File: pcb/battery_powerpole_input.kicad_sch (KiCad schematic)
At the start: 7 parts, among them J1 1377G12-BK, J2 MCV 1,5/ 2-GF-3,81

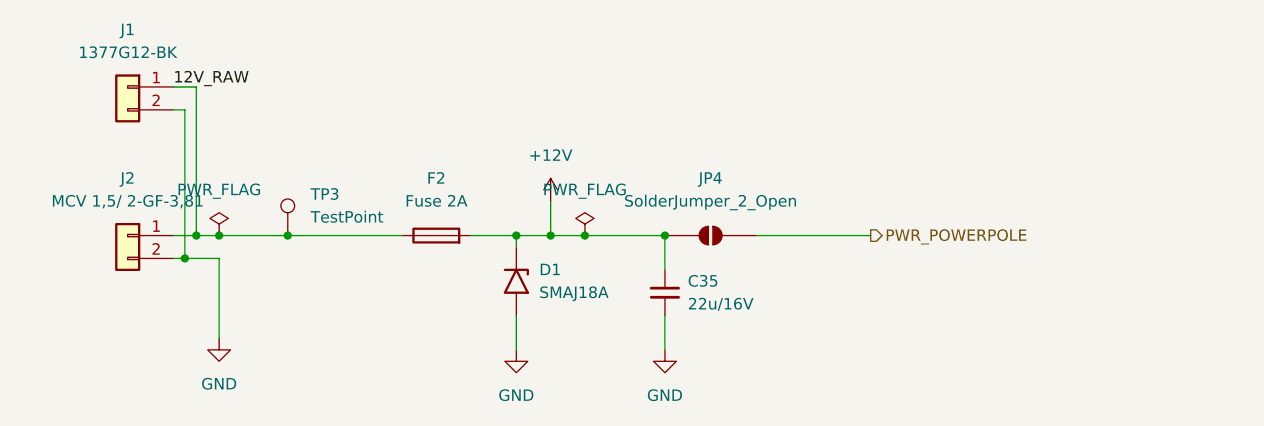
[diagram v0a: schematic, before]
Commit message: Add TPS2121 Stage 2/3: USB-vs-battery priority muxing on 5V and 3.3V rails
power.kicad_sch:
- U14 (TPS2121RUXR): 5V rail mux. IN1=BATT_5V_REG (priority), IN2=USB_5V_IN,
  OUT=+5V. PR1 tied to IN1, CP2/OV1/OV2 to GND (VREF priority mode -- battery
  always wins when present, no voltage-comparison ambiguity between two
  nominally-5V sources). ILM set via R26 (30.1k, ~3.5A class, sized with
  margin above the 2A SA818 budget for TX current transients). SS via C42
  (0.01uF). ST feeds the battery/USB detect logic below.
- U13 (TPS2121RUXR): 3.3V rail mux, same configuration. IN1=BATT_3.3V_REG,
  IN2=USB_3.3V_IN, OUT=+3.3V. ILM via R25 (80.6k, ~1.5A class, vs 1A
  peripheral budget). SS via C41.
- U1 (74LVC1G08): AND-gates U13.ST and U14.ST (each pulled up individually
  via R27/R28, 10k to +3.3V, since ST is open-drain) into PWR_ON_BATTERY --
  high only when both rails are confirmed running from battery, low if
  either has fallen back to USB. Output exposed as a new Power sheet pin.

foxhunt1.kicad_sch: bridges PWR_ON_BATTERY (Power sheet) to the new
IO_IN_ON_BATT input on the mcu-esp32 sheet, and USB_3.3V_IN/USB_5V_IN
(Power sheet) to USB_3.3V/USB_5V (USB-C sheet) -- these were previously
unconnected placeholder labels.

mcu-esp32.kicad_sch: IO_IN_ON_BATT wired to U8 pin 35 (GPIO42), the one
GPIO the pinout doc had marked as still spare.

kicad_gx_library: TPS2121RUXR symbol fix (one OUT pin marked passive
instead of output, since the two physical OUT pins are meant to be tied
together -- avoids an ERC driver-conflict false positive).

power_regulation.kicad_sch, battery_18650_input.kicad_sch,
battery_powerpole_input.kicad_sch, foxhunt1.kicad_pro: incidental KiCad
save cleanup, no circuit changes (verified via orphan/short checks and
netlist diff -- same components as before).

Fully traced pin-by-pin: both mux dividers/ILM/SS wiring, the battery-vs-
USB source assignment on each rail (not swapped), the AND-gate inputs,
and all three cross-sheet bridges. 0 new orpha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
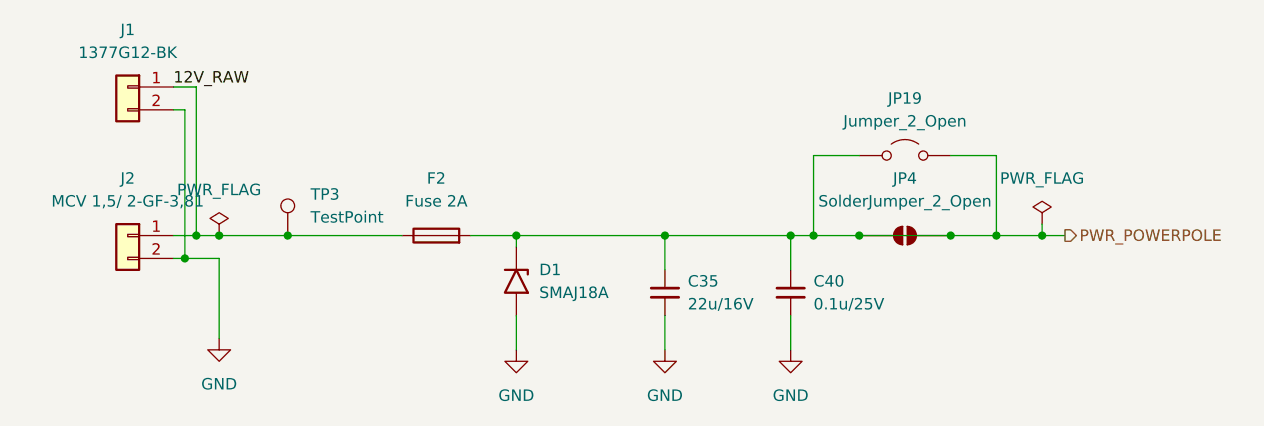
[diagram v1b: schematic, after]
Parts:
- added C40: 0.1u/25V, Capacitor_SMD:C_0603_1608Metric, symbol Device:C_Small
- added JP19: Jumper_2_Open, symbol Jumper:Jumper_2_Open
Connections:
- net +12V is gone; now on net PWR_POWERPOLE: C35.1, D1.1 (A1), F2.2, JP4.1 (A)
- net GND: now also C40.2
- net PWR_POWERPOLE: now also C40.1, JP19.1 (A), JP19.2 (B)
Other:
- moved on the sheet: JP4

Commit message: Full re-annotation, BOM audit fixes, Stage-1 ILM resize, and PCB reset
Schematic: re-annotated reference designators project-wide (3rd pass) --
every real component's designator has shifted since the last commit.
Fixed BOM gaps found by the fresh audit: U13 (CH340C) sourcing fields,
R7's Manf typo (YAGE -> YAGEO), R5/R8/R14 missing LCSC Part#s, and
normalized U1/U2/U3 (TPS2121RUXR) field names from easyeda2kicad's
defaults (Manufacturer/LCSC Part) to this project's convention
(Manf/LCSC Part #). Resized Stage 1's ILM resistor (R8) from 51.1k to
30.1k -- the prior value undersized the current limit for carrying both
downstream rails' combined battery-side current.

pcb/foxhunt1.kicad_pcb: cleared all footprints. No board layout has
started yet; this reflects that accurately rather than carrying stale
placements from before the schematic settled.

_agent_tasks/bom_property_audit.md: new reusable playbook for this BOM
audit (method, standing exceptions, reporting format), so future passes
don't have to re-derive the approach each time.

_docs/sourcing/task1_lcsc_crossreference.md: replaced stale results
(referencing pre-renumbering designators) with the current audit's
findings. One open item remains: the current-sense shunt's footprint
implies Vishay pad geometry but the sourced part is Milliohm-brand,
needs physical verification before fab.

Co-Authored-By: Claude Sonnet 5 <noreply@anthropic.com>
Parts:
- JP7: renamed from JP19; footprint (none) -> TestPoint:TestPoint_2Pads_Pitch2.54mm_Drill0.8mm
- renumbered C35 to C10, C40 to C11, JP4 to JP8
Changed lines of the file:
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@@
 		(dnp no)
 		(fields_autoplaced yes)
-		(property "Reference" "#PWR010"
+		(property "Reference" "#PWR036"
 			(at 67.31 97.79 0)
 			(hide yes)
@@
 			(project "foxhunt1"
 				(path "/8399ba4b-9428-480d-8b65-76cf154b97a5/37ac1273-0b70-4a42-ac28-8e382584c4a4/03f120c0-b388-4d10-bf8a-03d14068a336"
-					(reference "#PWR010")
+					(reference "#PWR036")
 					(unit 1)
 				)
@@
 		(dnp no)
 		(fields_autoplaced yes)
-		(property "Reference" "JP19"
+		(property "Reference" "JP7"
 			(at 143.51 64.77 0)
 			(show_name no)
@@
 			)
 		)
-		(property "Footprint" ""
+		(property "Footprint" "TestPoint:TestPoint_2Pads_Pitch2.54mm_Drill0.8mm"
 			(at 143.51 71.12 0)
 			(hide yes)
@@
 			(project "foxhunt1"
 				(path "/8399ba4b-9428-480d-8b65-76cf154b97a5/37ac1273-0b70-4a42-ac28-8e382584c4a4/03f120c0-b388-4d10-bf8a-03d14068a336"
-					(reference "JP19")
+					(reference "JP7")
 					(unit 1)
 				)
@@
 		(dnp no)
 		(fields_autoplaced yes)
-		(property "Reference" "#PWR011"
+		(property "Reference" "#PWR037"
 			(at 100.33 99.06 0)
 			(hide yes)
@@
 			(project "foxhunt1"
 				(path "/8399ba4b-9428-480d-8b65-76cf154b97a5/37ac1273-0b70-4a42-ac28-8e382584c4a4/03f120c0-b388-4d10-bf8a-03d14068a336"
-					(reference "#PWR011")
+					(reference "#PWR037")
 					(unit 1)
 				)
@@
 		(dnp no)
 		(fields_autoplaced yes)
-		(property "Reference" "#FLG07"
+		(property "Reference" "#FLG012"
 			(at 67.31 78.105 0)
 			(hide yes)
@@
 			(project "foxhunt1"
 				(path "/8399ba4b-9428-480d-8b65-76cf154b97a5/37ac1273-0b70-4a42-ac28-8e382584c4a4/03f120c0-b388-4d10-bf8a-03d14068a336"
-					(reference "#FLG07")
+					(reference "#FLG012")
 					(unit 1)
 				)
@@
 		(dnp no)
 		(fields_autoplaced yes)
-		(property "Reference" "#FLG08"
+		(property "Reference" "#FLG013"
 			(at 158.75 76.835 0)
 			(hide yes)
@@
 			(project "foxhunt1"
 				(path "/8399ba4b-9428-480d-8b65-76cf154b97a5/37ac1273-0b70-4a42-ac28-8e382584c4a4/03f120c0-b388-4d10-bf8a-03d14068a336"
-					(reference "#FLG08")
+					(reference "#FLG013")
 					(unit 1)
 				)
@@
 		(dnp no)
 		(fields_autoplaced yes)
-		(property "Reference" "#PWR069"
+		(property "Reference" "#PWR039"
 			(at 130.81 99.06 0)
 			(hide yes)
@@
 			(project "foxhunt1"
 				(path "/8399ba4b-9428-480d-8b65-76cf154b97a5/37ac1273-0b70-4a42-ac28-8e382584c4a4/03f120c0-b388-4d10-bf8a-03d14068a336"
-					(reference "#PWR069")
+					(reference "#PWR039")
 					(unit 1)
 				)
@@
 		(dnp no)
 		(fields_autoplaced yes)
-		(property "Reference" "C40"
+		(property "Reference" "C11"
 			(at 133.35 85.0899 0)
 			(show_name no)
@@
 			(project "foxhunt1"
 				(path "/8399ba4b-9428-480d-8b65-76cf154b97a5/37ac1273-0b70-4a42-ac28-8e382584c4a4/03f120c0-b388-4d10-bf8a-03d14068a336"
-					(reference "C40")
+					(reference "C11")
 					(unit 1)
 				)
@@
 		(dnp no)
 		(fields_autoplaced yes)
-		(property "Reference" "C35"
+		(property "Reference" "C10"
 			(at 119.38 85.0899 0)
 			(show_name no)
@@
 			(project "foxhunt1"
 				(path "/8399ba4b-9428-480d-8b65-76cf154b97a5/37ac1273-0b70-4a42-ac28-8e382584c4a4/03f120c0-b388-4d10-bf8a-03d14068a336"
-					(reference "C35")
+					(reference "C10")
 					(unit 1)
 				)
@@
 		(dnp no)
 		(fields_autoplaced yes)
-		(property "Reference" "#PWR058"
+		(property "Reference" "#PWR038"
 			(at 116.84 99.06 0)
 			(hide yes)
@@
 			(project "foxhunt1"
 				(path "/8399ba4b-9428-480d-8b65-76cf154b97a5/37ac1273-0b70-4a42-ac28-8e382584c4a4/03f120c0-b388-4d10-bf8a-03d14068a336"
-					(reference "#PWR058")
+					(reference "#PWR038")
 					(unit 1)
 				)
@@
 		(dnp no)
 		(fields_autoplaced yes)
-		(property "Reference" "JP4"
+		(property "Reference" "JP8"
 			(at 143.51 73.66 0)
 			(show_name no)
@@
 			(project "foxhunt1"
 				(path "/8399ba4b-9428-480d-8b65-76cf154b97a5/37ac1273-0b70-4a42-ac28-8e382584c4a4/03f120c0-b388-4d10-bf8a-03d14068a336"
-					(reference "JP4")
-					(unit 1)
-				)
+					(reference "JP8")
+					(unit 1)
+				)
